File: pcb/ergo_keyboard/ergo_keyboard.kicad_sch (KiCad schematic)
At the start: 0 parts

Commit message: working on schematic
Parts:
- added D1, D10, D11, D12, D13, D14, D15, D16, D17, D18, D19, D2, D20, D21, D22, D23, D3, D4, D5, D6, D7, D8, D9: Diode, symbol ScottoKeebs:Placeholder_Diode
- added LED1, LED10, LED11, LED12, LED13, LED14, LED15, LED16, LED17, LED18, LED19, LED2, LED20, LED21, LED22, LED23, LED3, LED4, LED5, LED6, LED7, LED8, LED9: SK6812MINI, LED_SMD:LED_SK6812MINI_PLCC4_3.5x3.5mm_P1.75mm, symbol LED:SK6812MINI
- added S1, S10, S11, S12, S13, S14, S15, S16, S17, S18, S19, S2, S20, S21, S22, S23, S3, S4, S5, S6, S7, S8, S9: Keyswitch, symbol ScottoKeebs:Placeholder_Keyswitch
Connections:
- new net: D19.2 (A), S19.2
- new net: D7.2 (A), S7.2
- new net: D13.2 (A), S13.2
- new net: D14.2 (A), S14.2
- new net: D21.2 (A), S21.2
- new net: LED20.1 (DOUT), LED23.3 (DIN)
- new net: LED15.1 (DOUT), LED20.3 (DIN)
- new net: D17.2 (A), S17.2
- new net: LED10.3 (DIN), LED5.1 (DOUT)
- new net: LED4.1 (DOUT), LED5.3 (DIN)
- new net: D15.2 (A), S15.2
- new net: D5.2 (A), S5.2
- new net: LED19.3 (DIN), LED22.1 (DOUT)
- new net: LED21.1 (DOUT), LED22.3 (DIN)
- new net: D18.2 (A), S18.2
- new net: D22.2 (A), S22.2
- new net: D16.2 (A), S16.2
- new net: LED4.3 (DIN), LED9.1 (DOUT)
- new net: LED14.1 (DOUT), LED9.3 (DIN)
- new net: D20.2 (A), S20.2
- new net: D1.2 (A), S1.2
- new net: LED2.3 (DIN), LED7.1 (DOUT)
- new net: LED12.1 (DOUT), LED7.3 (DIN)
- new net: LED10.1 (DOUT), LED15.3 (DIN)
- new net: D10.2 (A), S10.2
- new net: D4.2 (A), S4.2
- new net: D3.2 (A), S3.2
- new net: LED14.3 (DIN), LED19.1 (DOUT)
- new net: LED12.3 (DIN), LED17.1 (DOUT)
- new net: D6.2 (A), S6.2
- new net: LED18.1 (DOUT), LED21.3 (DIN)
- new net: LED13.1 (DOUT), LED18.3 (DIN)
- new net: LED13.3 (DIN), LED8.1 (DOUT)
- new net: LED3.1 (DOUT), LED8.3 (DIN)
- new net: LED11.1 (DOUT), LED16.3 (DIN)
- new net: LED11.3 (DIN), LED6.1 (DOUT)
- new net: LED16.1 (DOUT), LED17.3 (DIN)
- new net: D12.2 (A), S12.2
- new net: LED1.1 (DOUT), LED6.3 (DIN)
- new net: D2.2 (A), S2.2
- new net: LED2.1 (DOUT), LED3.3 (DIN)
- new net: D23.2 (A), S23.2
- new net: D11.2 (A), S11.2
- new net: D9.2 (A), S9.2
- new net: D8.2 (A), S8.2
- new net Col0: S1.1, S11.1, S16.1, S6.1
- new net Col1: S12.1, S17.1, S2.1, S7.1
- new net Col2: S13.1, S18.1, S21.1, S3.1, S8.1
- new net Col3: S14.1, S19.1, S22.1, S4.1, S9.1
- new net Col4: S10.1, S15.1, S20.1, S23.1, S5.1
- new net LED: LED1.3 (DIN)
- new net Row0: D1.1 (K), D2.1 (K), D3.1 (K), D4.1 (K), D5.1 (K)
- new net Row1: D10.1 (K), D6.1 (K), D7.1 (K), D8.1 (K), D9.1 (K)
- new net Row2: D11.1 (K), D12.1 (K), D13.1 (K), D14.1 (K), D15.1 (K)
- new net Row3: D16.1 (K), D17.1 (K), D18.1 (K), D19.1 (K), D20.1 (K)
- new net Row4: D21.1 (K), D22.1 (K), D23.1 (K)
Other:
- note added: "Dont forget level shifter"
- note added: "SN74LV1T34"

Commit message: still working on schematic
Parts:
- added C1: 100 uF, symbol Device:C
- added U1: SeeeduinoXIAO_BLE, zaphod:Seeeduino XIAO-MOUDLE14P-2.54-21X17.8MM, symbol Seeeduino XIAO:SeeeduinoXIAO_BLE
- added U2: 74HC595, symbol 74xx:74HC595
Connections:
- net Col0: now also U2.15 (QA)
- net Col1: now also U2.1 (QB)
- net Col2: now also U2.2 (QC)
- net Col3: now also U2.3 (QD)
- net Col4: now also U2.4 (QE)
- net Row0: now also U1.1 (PA02_A0_D0)
- net Row1: now also U1.2 (PA4_A1_D1)
- net Row2: now also U1.3 (PA10_A2_D2)
- net Row3: now also U1.4 (PA11_A3_D3), U1.5 (PA8_A4_D4_SDA)
- net GND: now reaches LED23.2 (VSS)
- net GND: now also LED1.2 (VSS), LED10.2 (VSS), LED11.2 (VSS), LED12.2 (VSS), LED13.2 (VSS), LED14.2 (VSS), LED15.2 (VSS), LED16.2 (VSS), LED17.2 (VSS), LED18.2 (VSS), LED19.2 (VSS), LED2.2 (VSS), LED20.2 (VSS), LED21.2 (VSS), LED22.2 (VSS), LED3.2 (VSS), LED4.2 (VSS), LED5.2 (VSS), LED6.2 (VSS), LED7.2 (VSS), LED8.2 (VSS), LED9.2 (VSS), C1.2, U1.13 (GND), U2.13 (~{OE}), U2.8 (GND)
- net +5V: now reaches LED23.4 (VDD)
- net +5V: now also LED1.4 (VDD), LED10.4 (VDD), LED11.4 (VDD), LED12.4 (VDD), LED13.4 (VDD), LED14.4 (VDD), LED15.4 (VDD), LED16.4 (VDD), LED17.4 (VDD), LED18.4 (VDD), LED19.4 (VDD), LED2.4 (VDD), LED20.4 (VDD), LED21.4 (VDD), LED22.4 (VDD), LED3.4 (VDD), LED4.4 (VDD), LED5.4 (VDD), LED6.4 (VDD), LED7.4 (VDD), LED8.4 (VDD), LED9.4 (VDD), C1.1, U1.14 (5V)
- new net +3V3: U1.12 (3V3), U2.10 (~{SRCLR}), U2.16 (VCC)
- new net MISO: U1.10 (PA5_A9_D9_MISO), U2.12 (RCLK)
- new net MOSI: U1.11 (PA6_A10_D10_MOSI), U2.14 (SER)
- new net SRCLK: U1.9 (PA7_A8_D8_SCK), U2.11 (SRCLK)
- no-connect marks 0 -> 4
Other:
- note added: "Keyboard Matrix"
- moved on the sheet: D1, D10, D11, D12, D13, D14, D15, D16, D17, D18, D19, D2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

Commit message: finishing up schematic
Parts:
- added BT1: Battery_Cell, symbol Device:Battery_Cell
- added LevelShifter: SN74LV1T34DBV, Package_TO_SOT_SMD:SOT-23-5, symbol Logic_LevelTranslator:SN74LV1T34DBV
- added SW1: SW_Push, symbol Switch:SW_Push
- added SW2: SW_SPDT, Button_Switch_SMD:SW_SPDT_PCM12, symbol Switch:SW_SPDT
- renumbered U1 to MCU, U2 to ShiftRegister
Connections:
- net +5V: now also LevelShifter.5 (VCC)
- net GND: now also LevelShifter.3 (GND), SW1.1, SW2.2 (B)
- net LED: now also LevelShifter.4 (Y)
- net 3v3 LED: now reaches MCU.6 (PA9_A5_D5_SCL)
- net 3v3 LED: now also LevelShifter.2 (A)
- new net: BT1.2 (-), SW2.1 (A)
- new net Bat+: BT1.1 (+)
- new net rst: SW1.2
- no-connect marks 4 -> 5
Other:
- note added: "Per Key RGB"
- note removed: "Dont forget level shifter"
- note removed: "SN74LV1T34"
- moved on the sheet: C1, LED1, LED10, LED11, LED12, LED13, LED14, LED15, LED16, LED17, LED18, LED19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

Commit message: 1st iteration of schematic done
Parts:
- removed D1, D10, D11, D12, D13, D14, D15, D16, D17, D18, D19, D2, D20, D21, D22, D23, D3, D4, D5, D6, D7, D8, D9: Diode, symbol ScottoKeebs:Placeholder_Diode
- removed S1, S10, S11, S12, S13, S14, S15, S16, S17, S18, S19, S2, S20, S21, S22, S23, S3, S4, S5, S6, S7, S8, S9: Keyswitch, symbol ScottoKeebs:Placeholder_Keyswitch
- added D1, D10, D11, D12, D13, D14, D15, D16, D17, D18, D19, D2, D20, D21, D22, D23, D24, D3, D4, D5, D6, D7, D8, D9: Diode, Diode_SMD:D_SOD-123, symbol Diode:1N4148W
- added SW10, SW11, SW12, SW13, SW14, SW15, SW16, SW17, SW18, SW19, SW20, SW21, SW22, SW23, SW3, SW4, SW5, SW6, SW7, SW8, SW9: Key Switch, symbol Switch:SW_Push_45deg
- added SW24: Program Btn, symbol Switch:SW_Push_45deg
- U2: renamed from ShiftRegister; value 74HC595 -> Shift Register
- U3: renamed from LevelShifter; value SN74LV1T34DBV -> Level Shifter
- renumbered SW1 to Sw25, SW2 to Sw26, MCU to U1
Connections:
- net rst is gone; now on net Rst: Sw25.2
- net Bat+: now also U1.16 (BAT+)
- net Col0: now also SW11.1, SW16.1, SW24.1, SW3.1, SW6.1
- net Col1: now also SW12.1, SW17.1, SW3.1, SW7.1
- net Col2: now also SW13.1, SW18.1, SW21.1, SW3.1, SW8.1
- net Col3: now also SW14.1, SW19.1, SW22.1, SW4.1, SW9.1
- net Col4: now also SW10.1, SW15.1, SW20.1, SW23.1, SW5.1
- net Row0: now also D1.1 (K), D2.1 (K), D3.1 (K), D4.1 (K), D5.1 (K)
- net Row1: now also D10.1 (K), D6.1 (K), D7.1 (K), D8.1 (K), D9.1 (K)
- net Row2: now also D11.1 (K), D12.1 (K), D13.1 (K), D14.1 (K), D15.1 (K)
- net Row3: now also D16.1 (K), D17.1 (K), D18.1 (K), D19.1 (K), D20.1 (K)
- net Row4: now also D21.1 (K), D22.1 (K), D23.1 (K), D24.1 (K)
- net Rst: now reaches U1.15 (RESET)
- new net: D4.2 (A), SW4.2
- new net: D9.2 (A), SW9.2
- new net: D13.2 (A), SW13.2
- new net: D22.2 (A), SW22.2
- new net: D6.2 (A), SW6.2
- new net: D5.2 (A), SW5.2
- new net: D23.2 (A), SW23.2
- new net: D3.2 (A), SW3.2
- new net: D14.2 (A), SW14.2
- new net: D11.2 (A), SW11.2
- new net: D18.2 (A), SW18.2
- new net: D21.2 (A), SW21.2
- new net: D24.2 (A), SW24.2
- new net: D15.2 (A), SW15.2
- new net: D10.2 (A), SW10.2
- new net: D7.2 (A), SW7.2
- new net: D16.2 (A), SW16.2
- new net: D17.2 (A), SW17.2
- new net: D12.2 (A), SW12.2
- new net: D2.2 (A), SW3.2
- new net: D8.2 (A), SW8.2
- new net: D19.2 (A), SW19.2
- new net: D1.2 (A), SW3.2
- new net: D20.2 (A), SW20.2
- no-connect marks 5 -> 6
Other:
- moved on the sheet: BT1, Sw25, Sw26, U1, U3

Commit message: fixed up schematic
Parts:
- added SW1, SW3: Key Switch, symbol Switch:SW_Push_45deg
- renumbered SW3 to SW2
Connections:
- net Col0: now also SW1.1; no longer SW2.1
- net Col2: now also SW3.1; no longer SW2.1
- net at D3.2 (A): now also SW3.2; no longer SW2.2
- net at D1.2 (A): now also SW1.2; no longer SW2.2
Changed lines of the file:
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@@
 	(wire
 		(pts
+			(xy 116.84 153.67) (xy 111.76 153.67)
+		)
+		(stroke
+			(width 0)
+			(type default)
+		)
+	)
+	(wire
+		(pts
 			(xy 77.47 29.21) (xy 77.47 34.29)
 		)
@@
 	(wire
 		(pts
-			(xy 111.76 153.67) (xy 118.11 153.67)
+			(xy 116.84 151.13) (xy 120.65 151.13)
 		)
 		(stroke
@@
 	(wire
 		(pts
+			(xy 116.84 151.13) (xy 116.84 153.67)
+		)
+		(stroke
+			(width 0)
+			(type default)
+		)
+	)
+	(wire
+		(pts
 			(xy 29.21 85.09) (xy 29.21 87.63)
 		)
@@
 	(symbol
 		(lib_id "power:GND")
-		(at 118.11 153.67 0)
+		(at 120.65 151.13 0)
 		(unit 1)
 		(exclude_from_sim no)
@@
 		(dnp no)
 		(property "Reference" "#PWR06"
-			(at 118.11 160.02 0)
+			(at 120.65 157.48 0)
 			(effects
 				(font
@@
 		)
 		(property "Value" "GND"
-			(at 118.11 157.48 0)
+			(at 120.65 154.94 0)
 			(effects
 				(font
@@
 		)
 		(property "Footprint" ""
-			(at 118.11 153.67 0)
+			(at 120.65 151.13 0)
 			(effects
 				(font
@@
 		)
 		(property "Datasheet" ""
-			(at 118.11 153.67 0)
+			(at 120.65 151.13 0)
 			(effects
 				(font
@@
 		)
 		(property "Description" "Power symbol creates a global label with name \"GND\" , ground"
-			(at 118.11 153.67 0)
+			(at 120.65 151.13 0)
 			(effects
 				(font

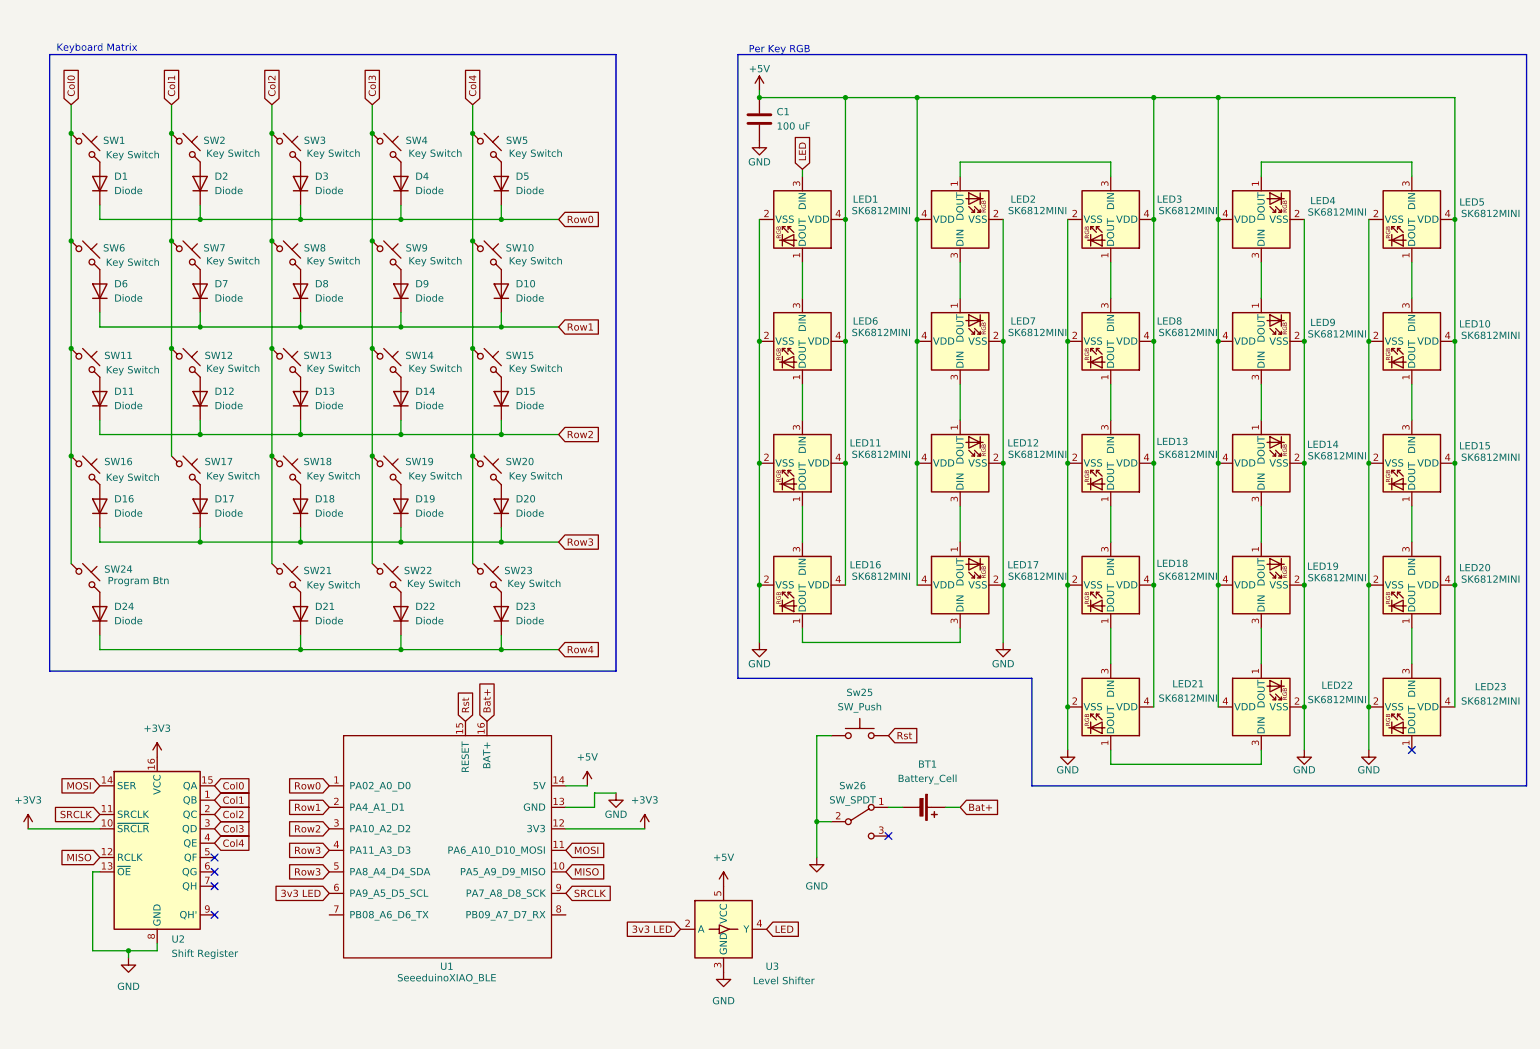
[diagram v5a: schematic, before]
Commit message: added usb interconnect for backlights
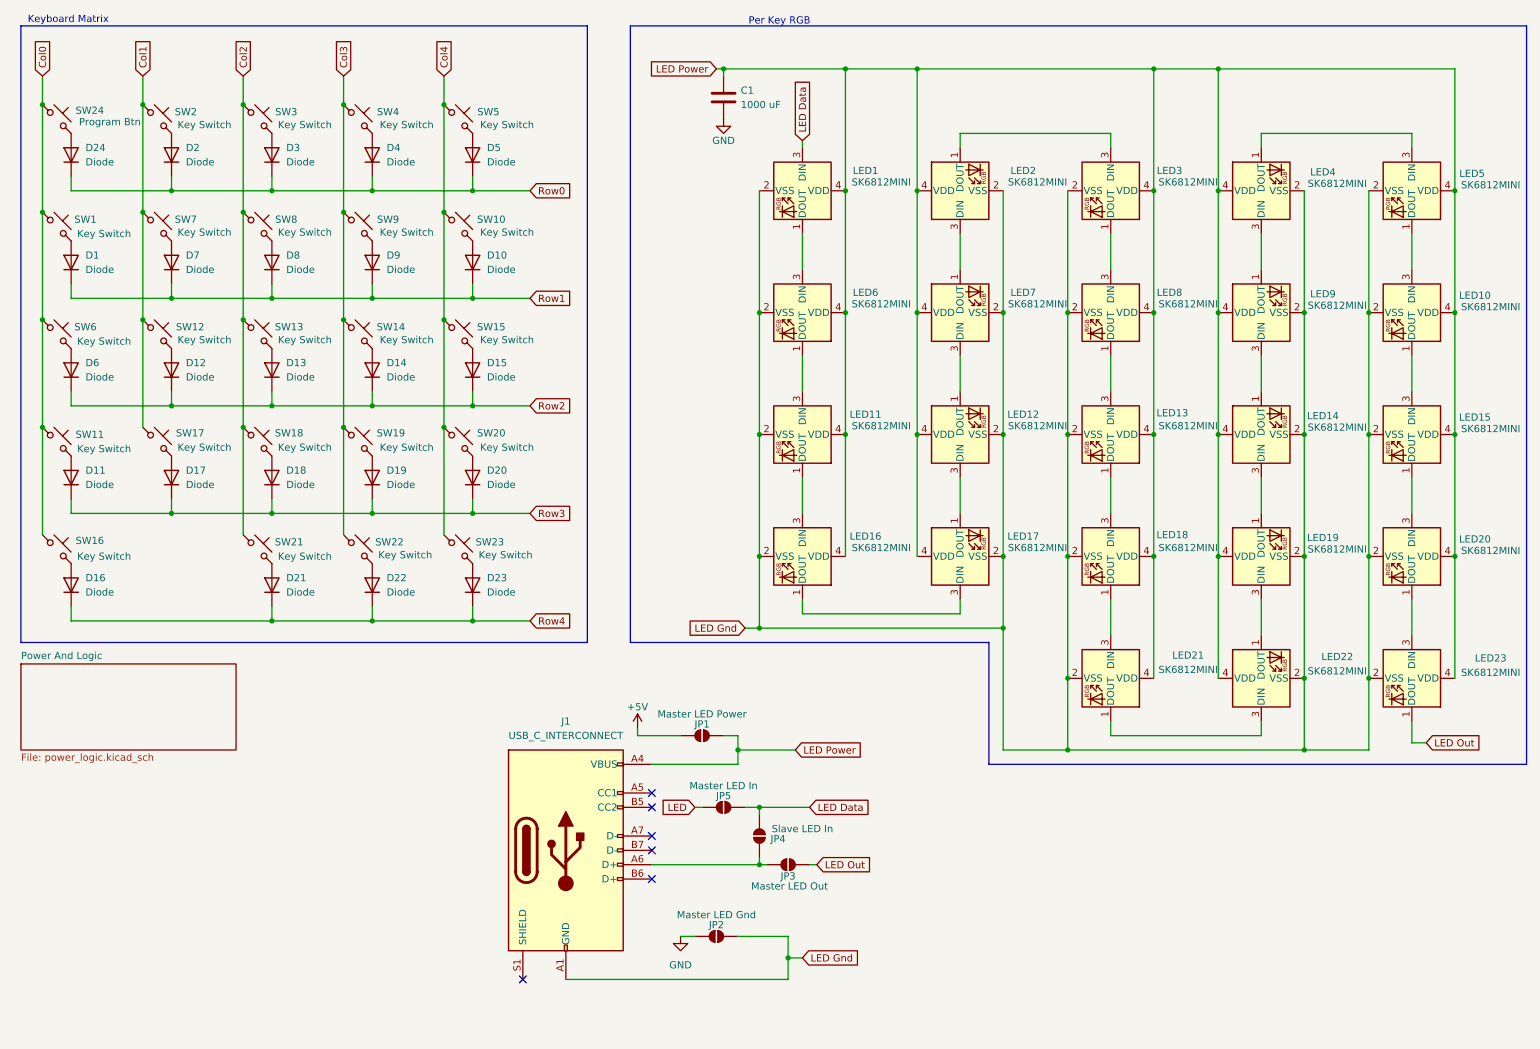
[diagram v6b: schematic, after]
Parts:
- removed BT1: Battery_Cell, symbol Device:Battery_Cell
- removed Sw25: SW_Push, symbol Switch:SW_Push
- removed Sw26: SW_SPDT, Button_Switch_SMD:SW_SPDT_PCM12, symbol Switch:SW_SPDT
- removed U1: SeeeduinoXIAO_BLE, zaphod:Seeeduino XIAO-MOUDLE14P-2.54-21X17.8MM, symbol Seeeduino XIAO:SeeeduinoXIAO_BLE
- removed U2: Shift Register, symbol 74xx:74HC595
- removed U3: Level Shifter, Package_TO_SOT_SMD:SOT-23-5, symbol Logic_LevelTranslator:SN74LV1T34DBV
- added J1: USB_C_INTERCONNECT, symbol Connector:USB_C_Receptacle_USB2.0_14P
- added JP1: Master LED Power, symbol Jumper:SolderJumper_2_Open
- added JP2: Master LED Gnd, symbol Jumper:SolderJumper_2_Open
- added JP3: Master LED Out, symbol Jumper:SolderJumper_2_Open
- added JP4: Slave LED In, symbol Jumper:SolderJumper_2_Open
- added JP5: Master LED In, symbol Jumper:SolderJumper_2_Open
- C1: value 100 uF -> 1000 uF
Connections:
- net +5V: now also JP1.1 (A); no longer C1.1, LED1.4 (VDD), LED10.4 (VDD), LED11.4 (VDD), LED12.4 (VDD), LED13.4 (VDD), LED14.4 (VDD), LED15.4 (VDD), LED16.4 (VDD), LED17.4 (VDD), LED18.4 (VDD), LED19.4 (VDD), LED2.4 (VDD), LED20.4 (VDD), LED21.4 (VDD), LED22.4 (VDD), LED23.4 (VDD), LED3.4 (VDD), LED4.4 (VDD), LED5.4 (VDD), LED6.4 (VDD), LED7.4 (VDD), LED8.4 (VDD), LED9.4 (VDD)
- net GND: now also JP2.2 (B); no longer LED1.2 (VSS), LED10.2 (VSS), LED11.2 (VSS), LED12.2 (VSS), LED13.2 (VSS), LED14.2 (VSS), LED15.2 (VSS), LED16.2 (VSS), LED17.2 (VSS), LED18.2 (VSS), LED19.2 (VSS), LED2.2 (VSS), LED20.2 (VSS), LED21.2 (VSS), LED22.2 (VSS), LED23.2 (VSS), LED3.2 (VSS), LED4.2 (VSS), LED5.2 (VSS), LED6.2 (VSS), LED7.2 (VSS), LED8.2 (VSS), LED9.2 (VSS)
- net LED: now also JP5.2 (B); no longer LED1.3 (DIN)
- net Row0: now also D24.1 (K); no longer D1.1 (K)
- net Row1: now also D1.1 (K); no longer D6.1 (K)
- net Row2: now also D6.1 (K); no longer D11.1 (K)
- net Row3: now also D11.1 (K); no longer D16.1 (K)
- net Row4: now also D16.1 (K); no longer D24.1 (K)
- net LED Out: now reaches LED23.1 (DOUT)
- net LED Out: now also JP3.2 (B)
- new net: J1.A6 (D+), JP3.1 (A), JP4.2 (B)
- new net LED Data: JP4.1 (A), JP5.1 (A), LED1.3 (DIN)
- new net LED Gnd: J1.A1 (GND), J1.A12 (GND), J1.B1 (GND), J1.B12 (GND), JP2.1 (A), LED1.2 (VSS), LED10.2 (VSS), LED11.2 (VSS), LED12.2 (VSS), LED13.2 (VSS), LED14.2 (VSS), LED15.2 (VSS), LED16.2 (VSS), LED17.2 (VSS), LED18.2 (VSS), LED19.2 (VSS), LED2.2 (VSS), LED20.2 (VSS), LED21.2 (VSS), LED22.2 (VSS), LED23.2 (VSS), LED3.2 (VSS), LED4.2 (VSS), LED5.2 (VSS), LED6.2 (VSS), LED7.2 (VSS), LED8.2 (VSS), LED9.2 (VSS)
- new net LED Power: C1.1, J1.A4 (VBUS), J1.A9 (VBUS), J1.B4 (VBUS), J1.B9 (VBUS), JP1.2 (B), LED1.4 (VDD), LED10.4 (VDD), LED11.4 (VDD), LED12.4 (VDD), LED13.4 (VDD), LED14.4 (VDD), LED15.4 (VDD), LED16.4 (VDD), LED17.4 (VDD), LED18.4 (VDD), LED19.4 (VDD), LED2.4 (VDD), LED20.4 (VDD), LED21.4 (VDD), LED22.4 (VDD), LED23.4 (VDD), LED3.4 (VDD), LED4.4 (VDD), LED5.4 (VDD), LED6.4 (VDD), LED7.4 (VDD), LED8.4 (VDD), LED9.4 (VDD)
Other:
- added sheet Power And Logic (power_logic.kicad_sch)
- moved on the sheet: C1, D1, D10, D11, D12, D13, D14, D15, D16, D17, D18, D19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
